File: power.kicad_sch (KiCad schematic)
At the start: 90 parts, among them U1 TPS546D24ARVFR, U3 TPSM861253RDXR, U4 TPS546D24ARVFR, U5 L78L05_SOT89

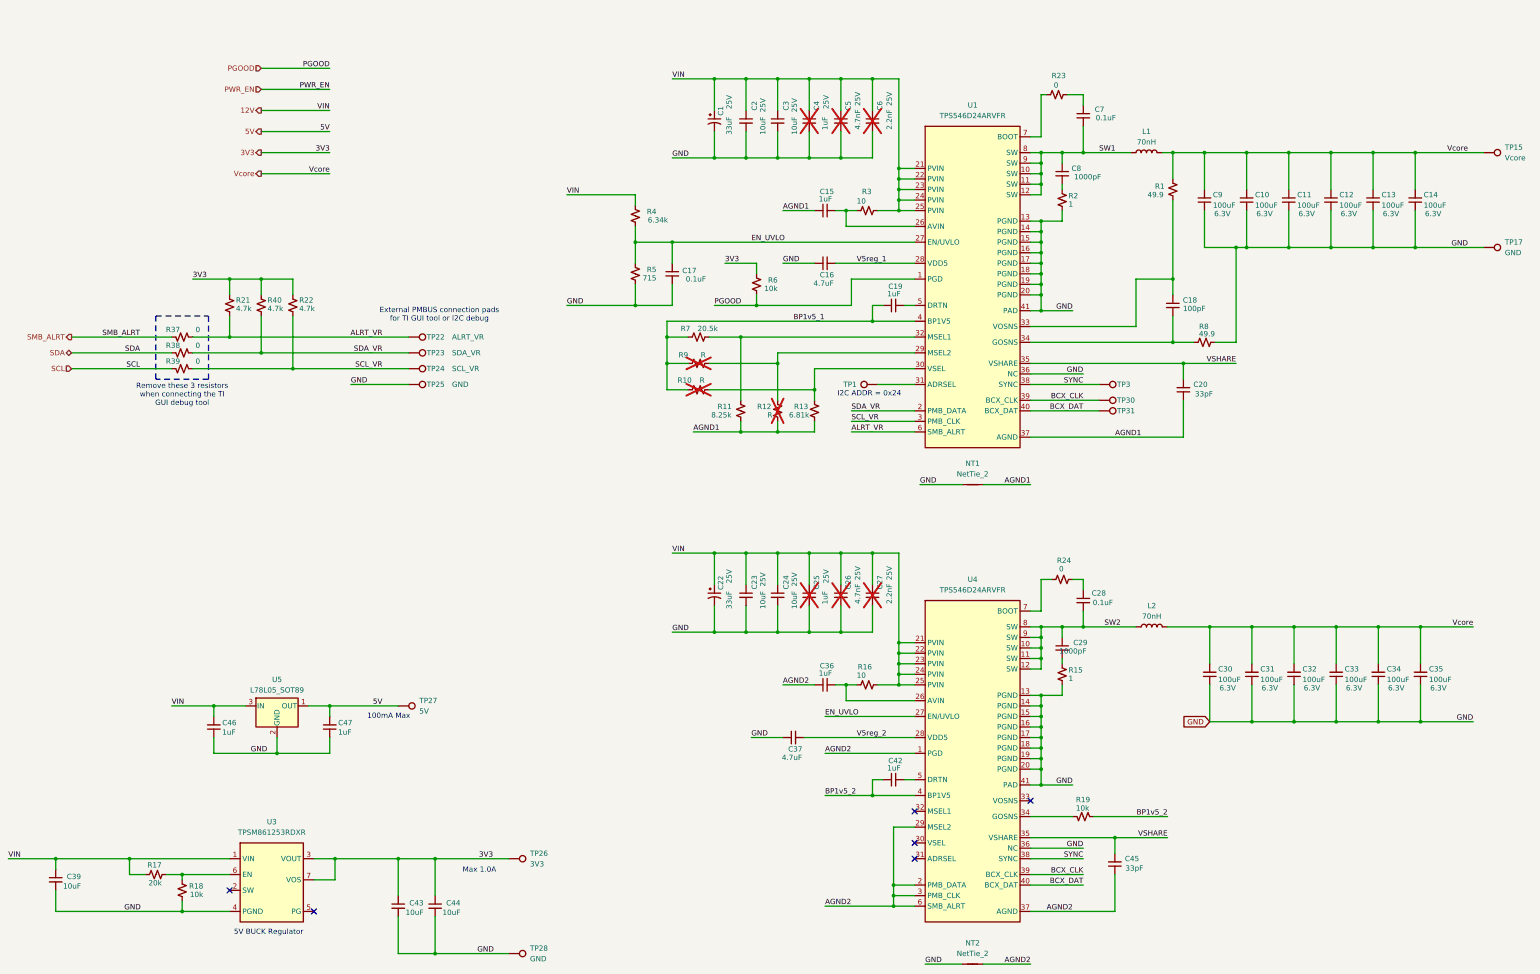
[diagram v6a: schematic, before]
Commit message: made the board double wide. rough ASIC and vreg placement.
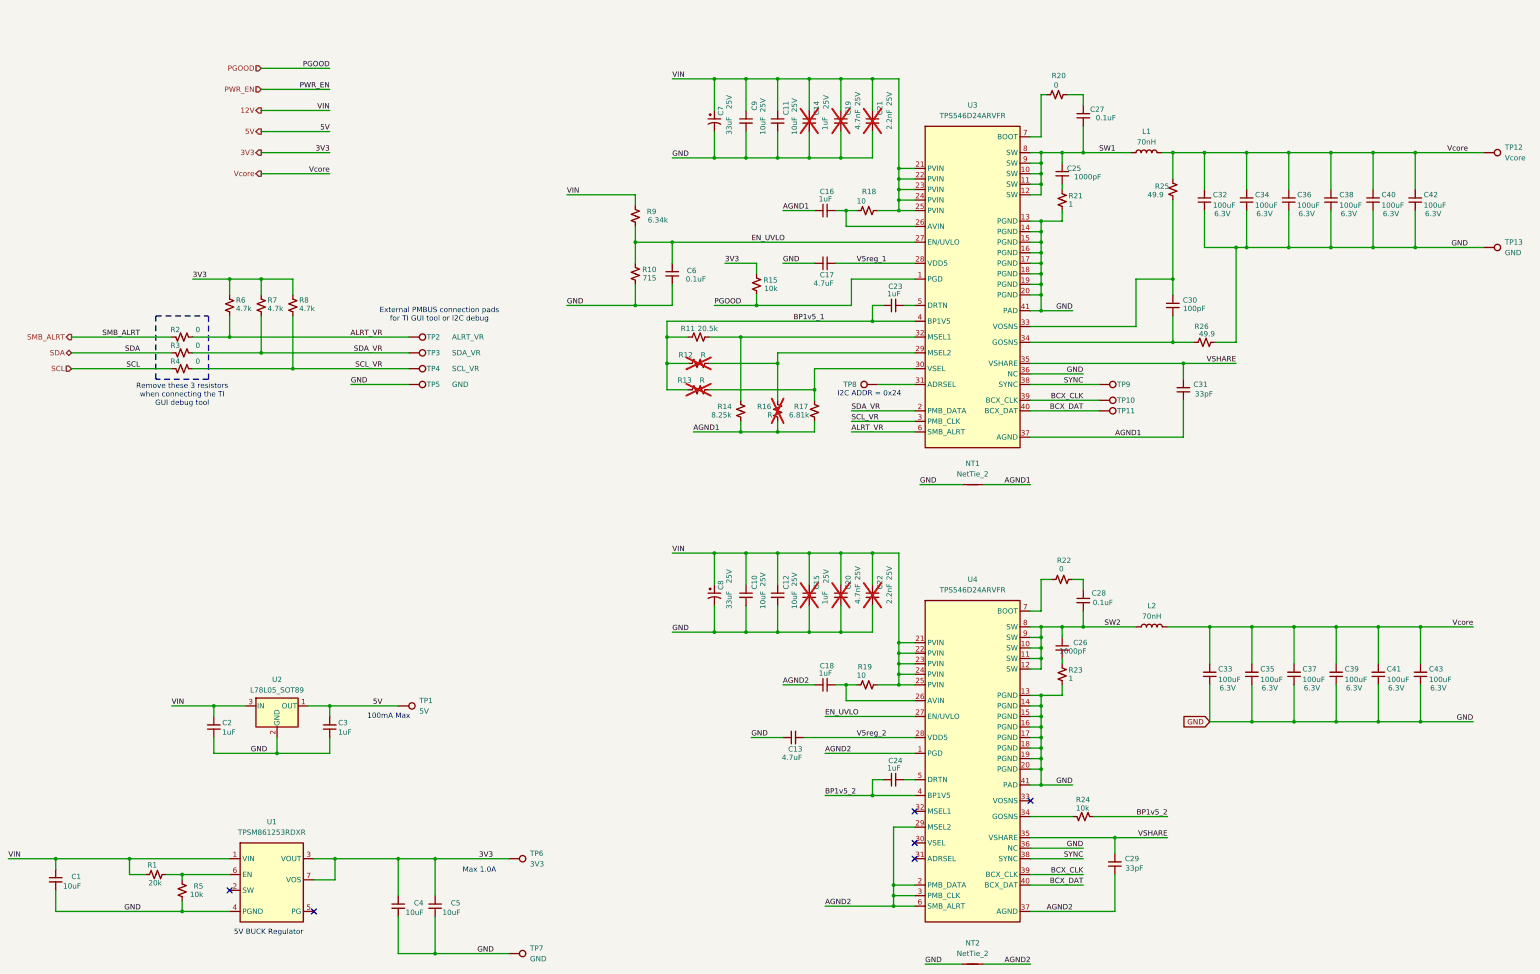
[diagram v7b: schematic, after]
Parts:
- renumbered C39 to C1, C23 to C10, C3 to C11, C24 to C12, C37 to C13, C4 to C14, C25 to C15, C15 to C16, C16 to C17, C36 to C18, C5 to C19, C46 to C2, C26 to C20, C6 to C21, C27 to C22, C19 to C23, C42 to C24, C8 to C25, C29 to C26, C7 to C27, C45 to C29, C47 to C3, C18 to C30, C20 to C31, C9 to C32, C30 to C33, C10 to C34, C31 to C35, C11 to C36, C32 to C37, C12 to C38, C33 to C39, C43 to C4, C13 to C40, C34 to C41, C14 to C42, C35 to C43, C44 to C5, C17 to C6, C1 to C7, C22 to C8, C2 to C9, R17 to R1, R5 to R10, R7 to R11, R9 to R12, R10 to R13, R11 to R14, R6 to R15, R12 to R16, R13 to R17, R3 to R18, R16 to R19, R37 to R2, R23 to R20, R2 to R21, R24 to R22, R15 to R23, R19 to R24, R1 to R25, R8 to R26, R38 to R3, R39 to R4, R18 to R5, R21 to R6, R40 to R7, R22 to R8, R4 to R9, TP27 to TP1, TP30 to TP10, TP31 to TP11, TP15 to TP12, TP17 to TP13, TP22 to TP2, TP23 to TP3, TP24 to TP4, TP25 to TP5, TP26 to TP6, TP28 to TP7, TP1 to TP8, TP3 to TP9, U3 to U1, U5 to U2, U1 to U3

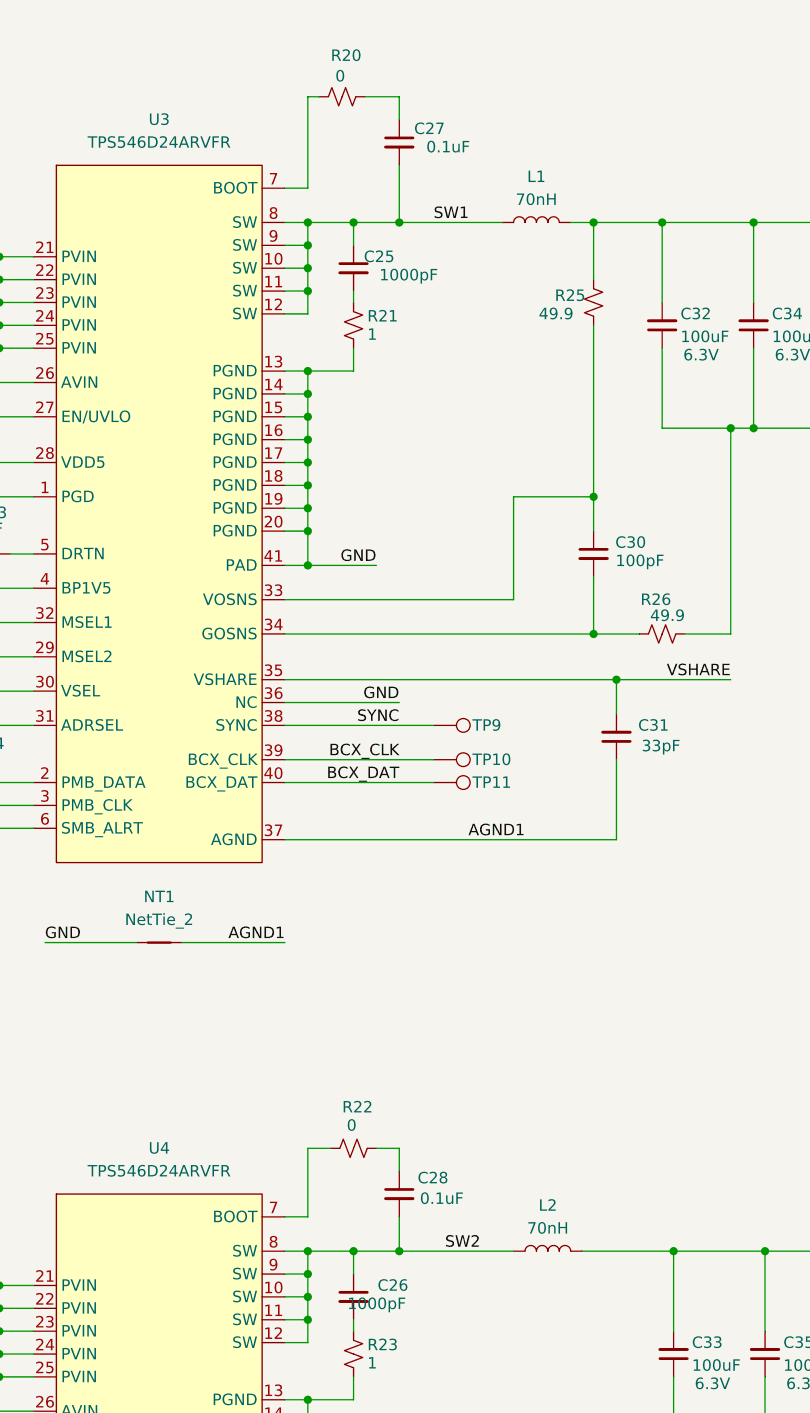
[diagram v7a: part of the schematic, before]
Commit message: ASICs placed. most other parts placed.
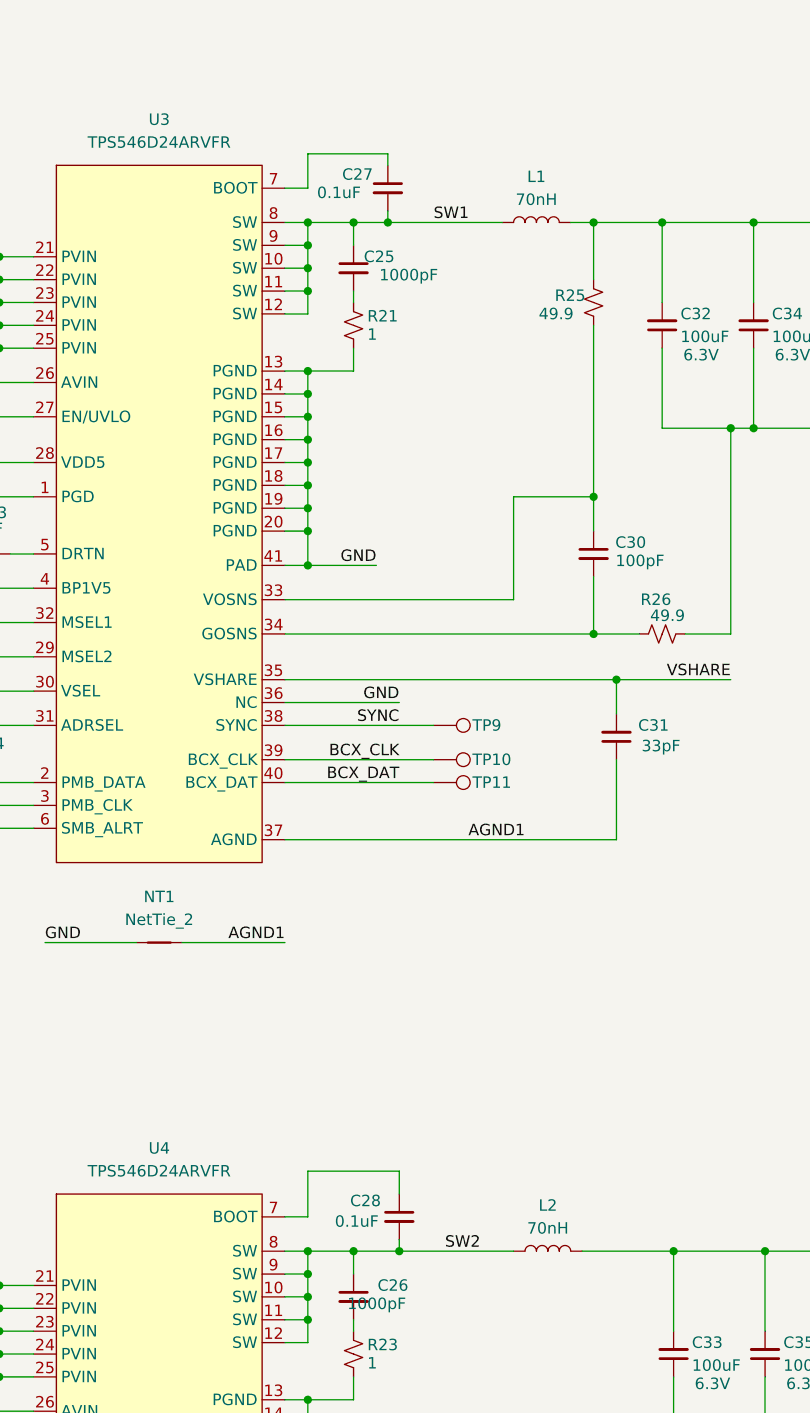
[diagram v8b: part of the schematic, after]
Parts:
- removed R20, R22: 0, Resistor_SMD:R_0402_1005Metric, symbol Device:R_Small_US
- R12, R13, R16: now left out of the parts list
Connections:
- net at C28.1: now also U4.7 (BOOT)
- net at U3.7 (BOOT): now also C27.1
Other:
- moved on the sheet: C27, C28
